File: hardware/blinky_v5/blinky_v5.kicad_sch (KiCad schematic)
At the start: 235 parts, among them J1 RJ45, J10 Conn_01x04, J11 Conn_01x08, J12 Conn_01x06, J2 Conn_01x06_Pin, J3 Conn_01x05_Pin, J5 Conn_01x06_Pin, J6 Conn_01x04_Pin, J7 Conn_01x04_Pin, J8 Conn_01x02, J9 Conn_02x10_Odd_Even, Q1 2N7002, Q2 2N7002, Q3 2N7002, Q4 2N7002, Q5 2N7002, Q6 2N7002, Q7 2N7002, Q8 2N7002, U1 ADA4807-1, U10 STM32F405RGTx, U11 AMS1117-3.3, U12 BA50DD0WHFP-TR, U13 M24C02-RMN, U2 SN74LVC1G14DBV, U3 SN74LVC1G14DBV, U4 ADA4807-1, U5 ADA4807-1, U6 TLV3603DCKR, U7 SN74LVC1G14DBV, U8 TLV3603DCKR, U9 L78L05_SOT89, X1 GTXO-14V (2.048MHz), X2 GTXO-14V (2.048MHz), Y1 AOCJY4A-10.000MHZ-SW, Y2 16MHz

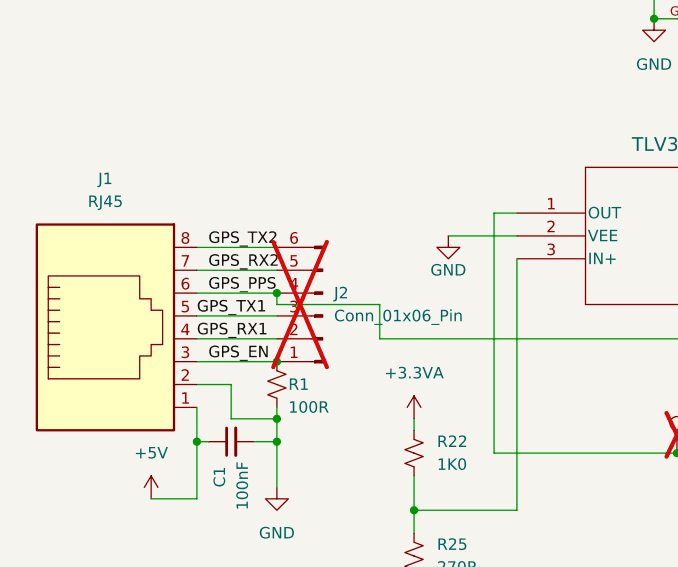
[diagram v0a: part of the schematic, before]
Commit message: fix GPS PPS routing bug
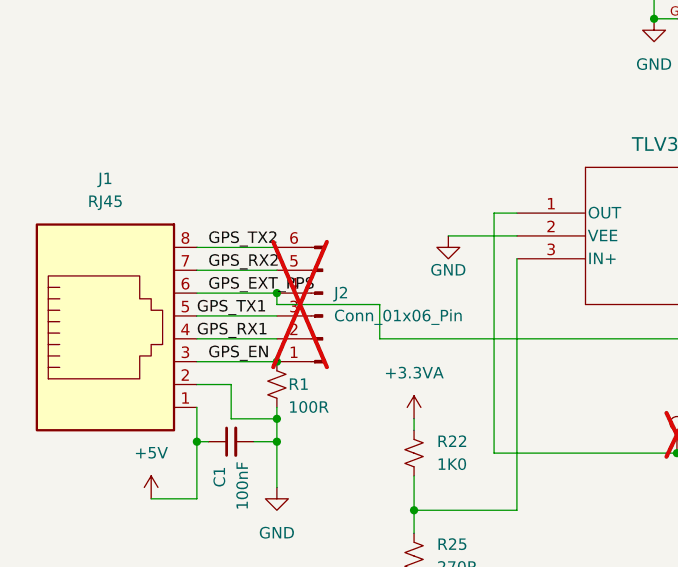
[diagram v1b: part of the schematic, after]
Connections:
- net GPS_PPS: no longer J1.6, J2.4 (Pin_4), U8.4 (IN-)
- new net GPS_EXT_PPS: J1.6, J2.4 (Pin_4), U8.4 (IN-)

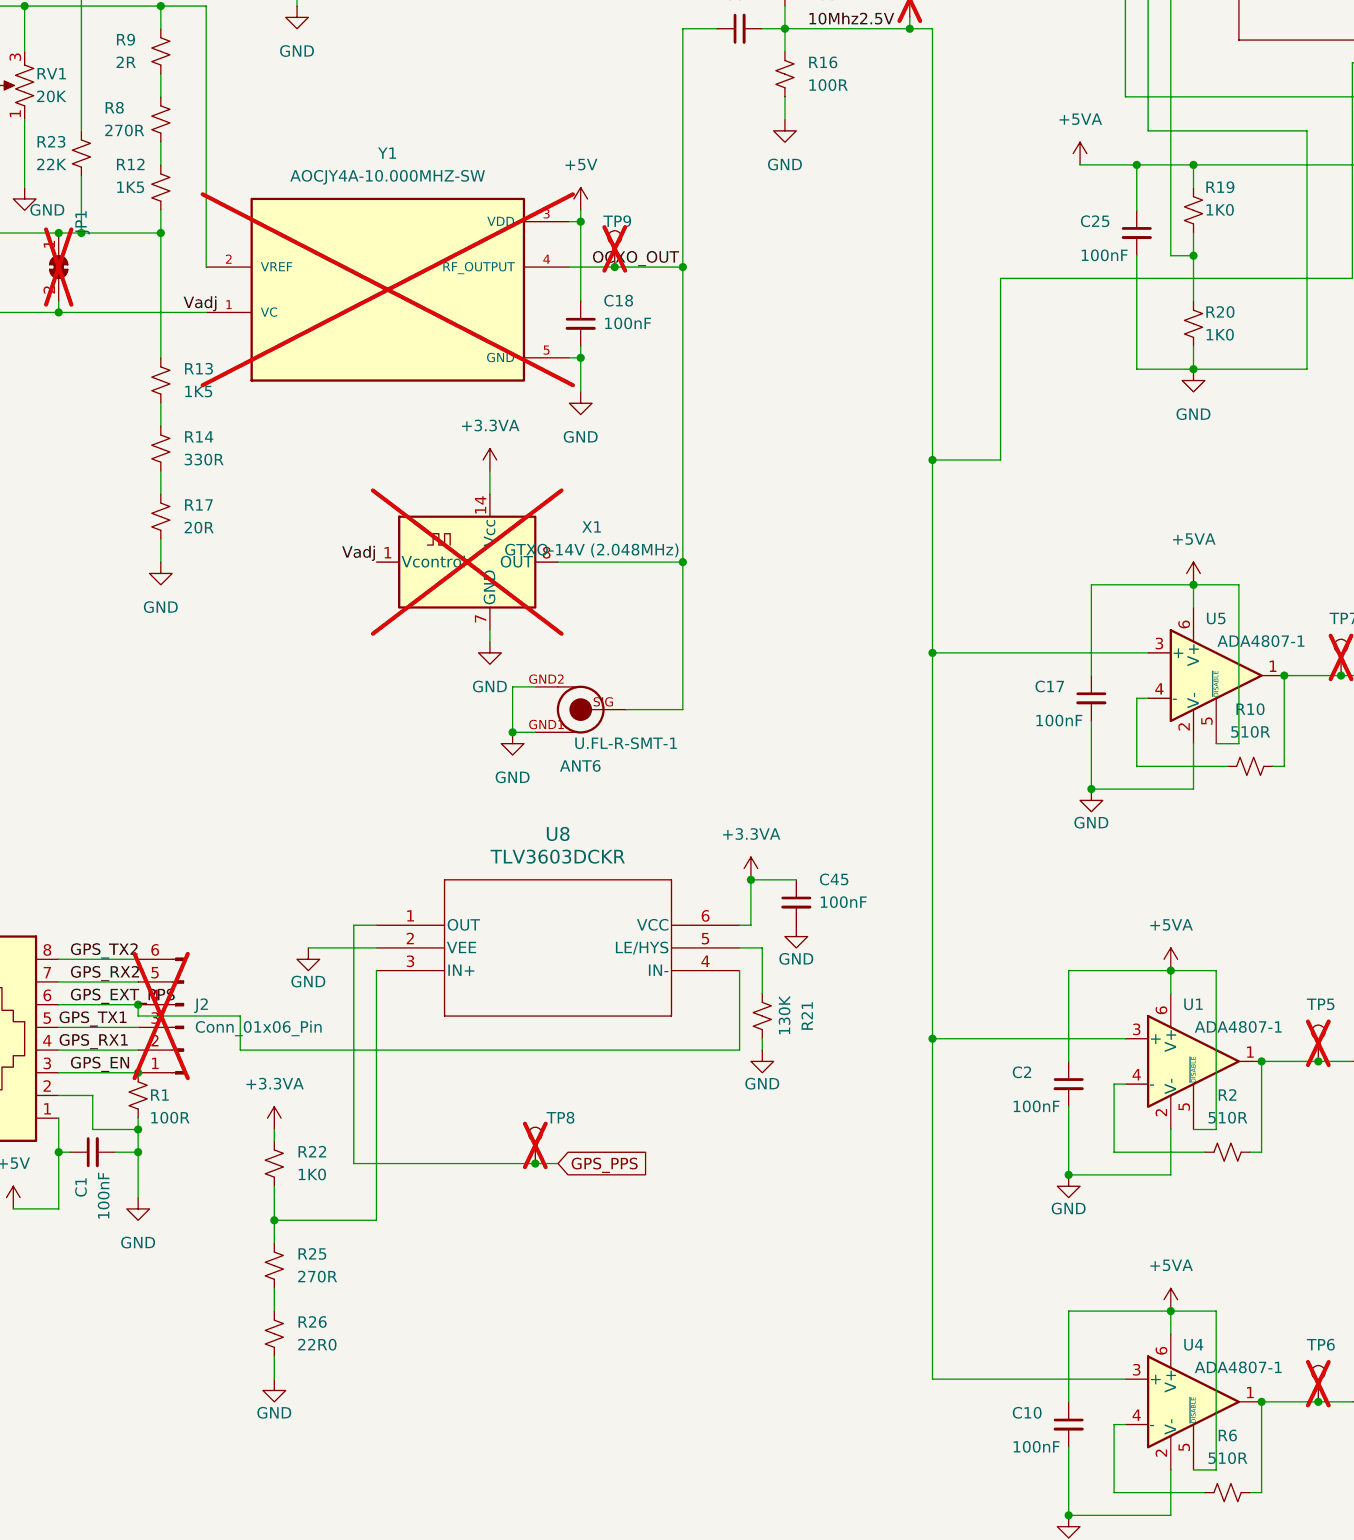
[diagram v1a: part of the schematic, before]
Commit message: filter power splits
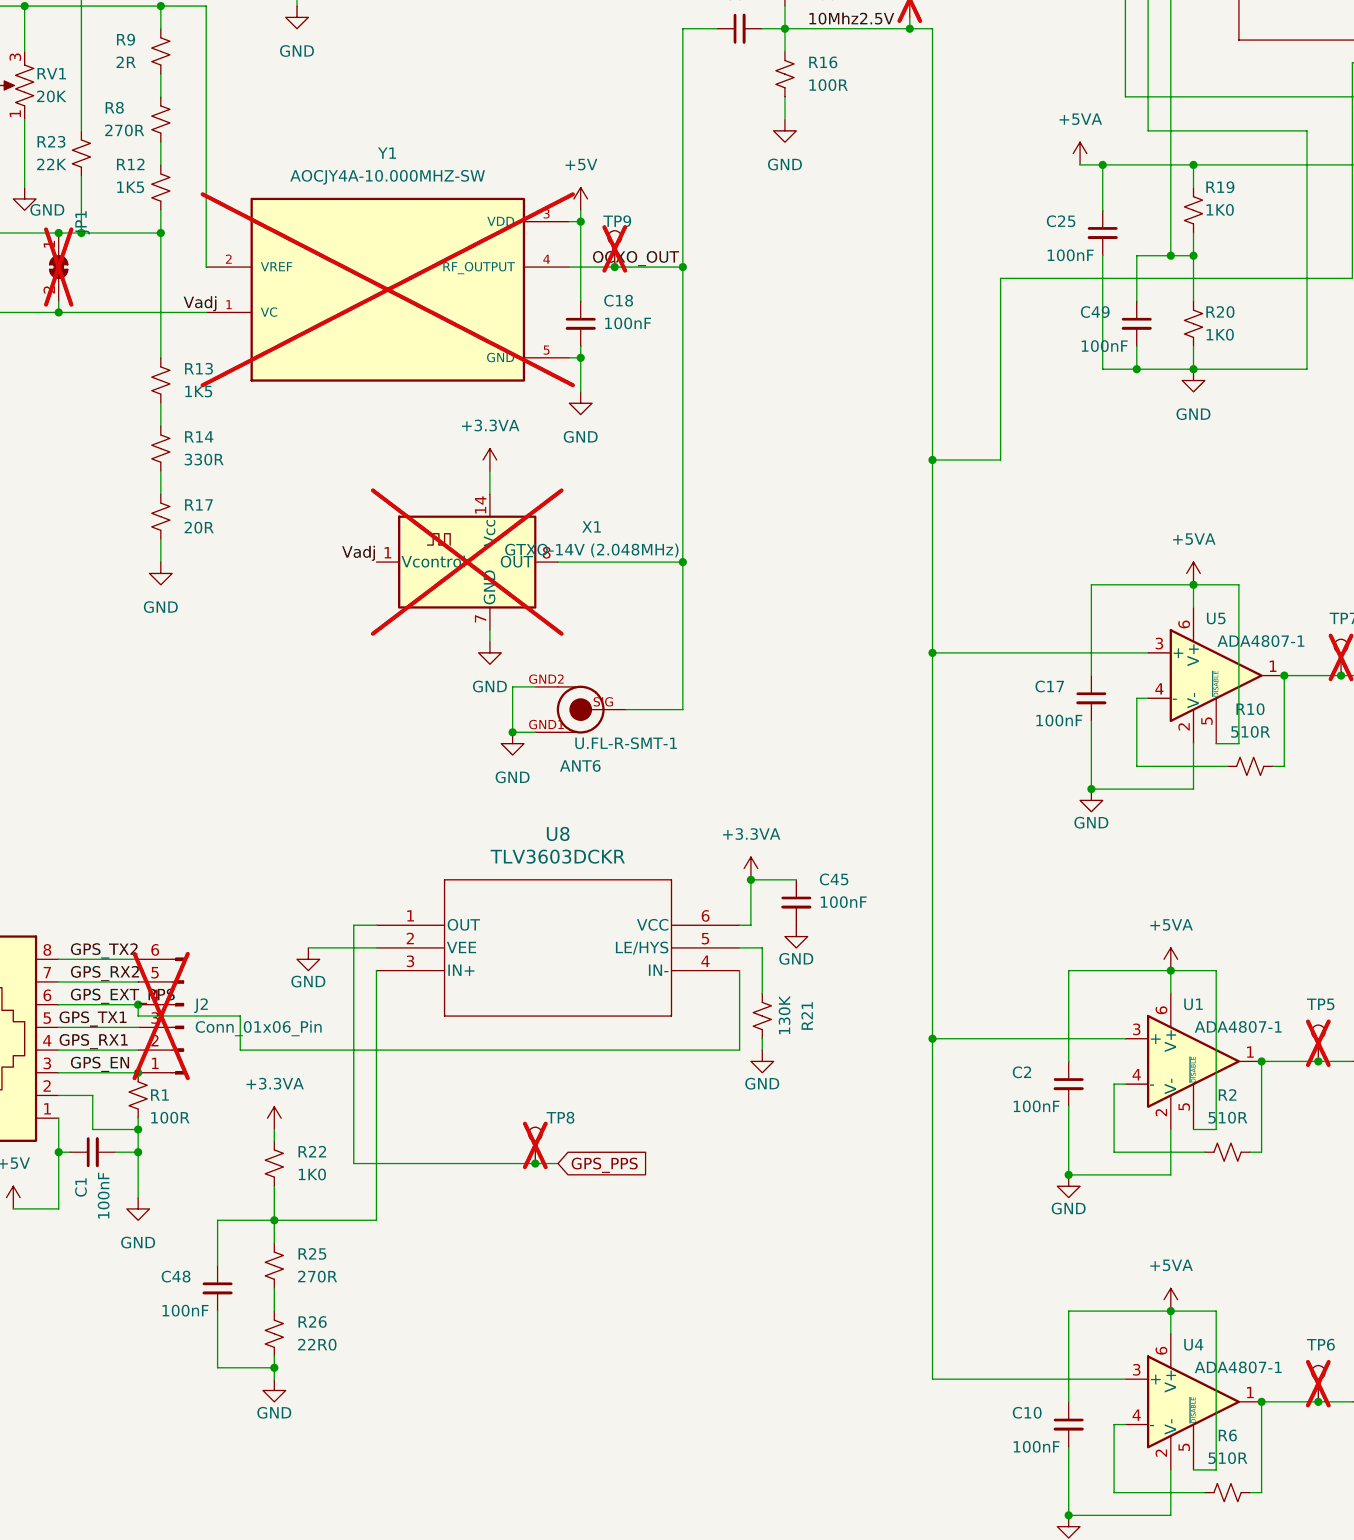
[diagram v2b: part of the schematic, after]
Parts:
- added C48, C49: 100nF, Capacitor_SMD:C_0402_1005Metric, symbol Device:C_Small
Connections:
- net GND: now also C48.2, C49.2
- net at R22.2, R25.1, U8.3 (IN+): now also C48.1
- net at R19.2, R20.1, U6.3 (IN+): now also C49.1
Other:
- moved on the sheet: C25
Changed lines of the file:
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@@
   (junction (at 393.7 132.08) (diameter 0) (color 0 0 0 0)
   )
+  (junction (at 151.13 247.65) (diameter 0) (color 0 0 0 0)
+  )
   (junction (at 359.41 201.93) (diameter 0) (color 0 0 0 0)
   )
@@
   (junction (at 36.83 220.98) (diameter 0) (color 0 0 0 0)
   )
-  (junction (at 154.94 247.65) (diameter 0) (color 0 0 0 0)
-  )
   (junction (at 373.38 132.08) (diameter 0) (color 0 0 0 0)
   )
@@
   (junction (at 308.61 388.62) (diameter 0) (color 0 0 0 0)
   )
+  (junction (at 154.94 270.51) (diameter 0) (color 0 0 0 0)
+  )
   (junction (at 161.29 257.81) (diameter 0) (color 0 0 0 0)
   )
@@
   (junction (at 383.54 132.08) (diameter 0) (color 0 0 0 0)
   )
+  (junction (at 58.42 382.27) (diameter 0) (color 0 0 0 0)
+  )
   (junction (at 288.29 80.01) (diameter 0) (color 0 0 0 0)
   )
   (junction (at 359.41 170.18) (diameter 0) (color 0 0 0 0)
   )
+  (junction (at 158.75 257.81) (diameter 0) (color 0 0 0 0)
+  )
   (junction (at 359.41 215.9) (diameter 0) (color 0 0 0 0)
   )
@@
     (stroke (width 0) (type default))
   )
-  (wire (pts (xy 154.94 247.65) (xy 148.59 247.65))
-    (stroke (width 0) (type default))
-  )
-  (wire (pts (xy 154.94 257.81) (xy 154.94 270.51))
+  (wire (pts (xy 151.13 257.81) (xy 151.13 270.51))
     (stroke (width 0) (type default))
   )
@@
     (stroke (width 0) (type default))
   )
+  (wire (pts (xy 154.94 270.51) (xy 161.29 270.51))
+    (stroke (width 0) (type default))
+  )
   (wire (pts (xy 302.26 295.91) (xy 302.26 298.45))
     (stroke (width 0) (type default))
@@
     (stroke (width 0) (type default))
   )
+  (wire (pts (xy 151.13 247.65) (xy 161.29 247.65))
+    (stroke (width 0) (type default))
+  )
   (wire (pts (xy 332.74 275.59) (xy 334.01 275.59))
     (stroke (width 0) (type default))
@@
     (stroke (width 0) (type default))
   )
+  (wire (pts (xy 154.94 267.97) (xy 154.94 270.51))
+    (stroke (width 0) (type default))
+  )
   (wire (pts (xy 39.37 139.7) (xy 40.64 139.7))
     (stroke (width 0) (type default))
@@
     (stroke (width 0) (type default))
   )
+  (wire (pts (xy 58.42 382.27) (xy 58.42 383.54))
+    (stroke (width 0) (type default))
+  )
   (wire (pts (xy 66.04 86.36) (xy 66.04 87.63))
     (stroke (width 0) (type default))
@@
     (stroke (width 0) (type default))
   )
-  (wire (pts (xy 154.94 270.51) (xy 161.29 270.51))
+  (wire (pts (xy 151.13 270.51) (xy 154.94 270.51))
     (stroke (width 0) (type default))
   )
@@
     (stroke (width 0) (type default))
   )
+  (wire (pts (xy 154.94 257.81) (xy 158.75 257.81))
+    (stroke (width 0) (type default))
+  )
   (wire (pts (xy 363.22 233.68) (xy 355.6 233.68))
     (stroke (width 0) (type default))
@@
     (stroke (width 0) (type default))
   )
+  (wire (pts (xy 52.07 370.84) (xy 52.07 365.76))
+    (stroke (width 0) (type default))
+  )
   (wire (pts (xy 147.32 353.06) (xy 147.32 360.68))
     (stroke (width 0) (type default))
@@
     (stroke (width 0) (type default))
   )
+  (wire (pts (xy 52.07 375.92) (xy 52.07 382.27))
+    (stroke (width 0) (type default))
+  )
   (wire (pts (xy 92.71 254) (xy 92.71 262.89))
     (stroke (width 0) (type default))
@@
     (stroke (width 0) (type default))
   )
+  (wire (pts (xy 52.07 382.27) (xy 58.42 382.27))
+    (stroke (width 0) (type default))
+  )
   (wire (pts (xy 163.83 393.7) (xy 163.83 375.92))
     (stroke (width 0) (type default))
@@
     (stroke (width 0) (type default))
   )
-  (wire (pts (xy 58.42 381) (xy 58.42 383.54))
+  (wire (pts (xy 58.42 381) (xy 58.42 382.27))
     (stroke (width 0) (type default))
   )
@@
     (stroke (width 0) (type default))
   )
+  (wire (pts (xy 154.94 262.89) (xy 154.94 257.81))
+    (stroke (width 0) (type default))
+  )
   (wire (pts (xy 383.54 168.91) (xy 378.46 168.91))
     (stroke (width 0) (type default))
@@
     (stroke (width 0) (type default))
   )
-  (wire (pts (xy 154.94 247.65) (xy 161.29 247.65))
-    (stroke (width 0) (type default))
-  )
   (wire (pts (xy 166.37 294.64) (xy 161.29 294.64))
     (stroke (width 0) (type default))
@@
     (stroke (width 0) (type default))
   )
+  (wire (pts (xy 151.13 247.65) (xy 148.59 247.65))
+    (stroke (width 0) (type default))
+  )
   (wire (pts (xy 320.04 27.94) (xy 320.04 30.48))
     (stroke (width 0) (type default))
@@
     (stroke (width 0) (type default))
   )
+  (wire (pts (xy 52.07 365.76) (xy 58.42 365.76))
+    (stroke (width 0) (type default))
+  )
   (wire (pts (xy 45.72 245.11) (xy 45.72 247.65))
     (stroke (width 0) (type default))
@@
     (stroke (width 0) (type default))
   )
-  (wire (pts (xy 154.94 252.73) (xy 154.94 247.65))
+  (wire (pts (xy 151.13 252.73) (xy 151.13 247.65))
     (stroke (width 0) (type default))
   )
@@
     )
   )
+  (symbol (lib_id "Device:C_Small") (at 52.07 373.38 0) (unit 1)
+    (in_bom yes) (on_board yes) (dnp no)
+    (property "Reference" "C48" (at 45.72 372.11 0)
+      (effects (font (size 1.27 1.27)) (justify left))
+    )
+    (property "Value" "100nF" (at 45.72 375.92 0)
+      (effects (font (size 1.27 1.27)) (justify left))
+    )
+    (property "Footprint" "Capacitor_SMD:C_0402_1005Metric" (at 52.07 373.38 0)
+      (effects (font (size 1.27 1.27)) hide)
+    )
+    (property "Datasheet" "https://www.mouser.ca/datasheet/2/447/UPY_GPHC_X7R_6_3V_to_250V_23-3084653.pdf" (at 52.07 373.38 0)
+      (effects (font (size 1.27 1.27)) hide)
+    )
+    (property "LCSC" "C307331" (at 52.07 373.38 0)
+      (effects (font (size 1.27 1.27)) hide)
+    )
+    (pin "1")
+    (pin "2")
+    (instances
+      (project "blinky_v5"
+        (path "/bd4d3b9a-07c1-4a53-9c94-2893f3e869d4"
+          (reference "C48") (unit 1)
+        )
+      )
+    )
+  )
   (symbol (lib_id "Device:LED") (at 289.56 35.56 90) (unit 1)
     (in_bom yes) (on_board yes) (dnp no) (fields_autoplaced)
@@
     )
   )
-  (symbol (lib_id "Device:C_Small") (at 154.94 255.27 0) (unit 1)
+  (symbol (lib_id "Device:C_Small") (at 151.13 255.27 0) (unit 1)
     (in_bom yes) (on_board yes) (dnp no)
-    (property "Reference" "C25" (at 148.59 254 0)
+    (property "Reference" "C25" (at 144.78 254 0)
       (effects (font (size 1.27 1.27)) (justify left))
     )
-    (property "Value" "100nF" (at 148.59 257.81 0)
+    (property "Value" "100nF" (at 144.78 257.81 0)
       (effects (font (size 1.27 1.27)) (justify left))
     )
-    (property "Footprint" "Capacitor_SMD:C_0402_1005Metric" (at 154.94 255.27 0)
+    (property "Footprint" "Capacitor_SMD:C_0402_1005Metric" (at 151.13 255.27 0)
       (effects (font (size 1.27 1.27)) hide)
     )
-    (property "Datasheet" "https://www.mouser.ca/datasheet/2/447/UPY_GPHC_X7R_6_3V_to_250V_23-3084653.pdf" (at 154.94 255.27 0)
+    (property "Datasheet" "https://www.mouser.ca/datasheet/2/447/UPY_GPHC_X7R_6_3V_to_250V_23-3084653.pdf" (at 151.13 255.27 0)
       (effects (font (size 1.27 1.27)) hide)
     )
-    (property "LCSC" "C307331" (at 154.94 255.27 0)
+    (property "LCSC" "C307331" (at 151.13 255.27 0)
       (effects (font (size 1.27 1.27)) hide)
     )
@@
         )
       )
+    )
+  )
+  (symbol (lib_id "Device:C_Small") (at 154.94 265.43 0) (unit 1)
+    (in_bom yes) (on_board yes) (dnp no)
+    (property "Reference" "C49" (at 148.59 264.16 0)
+      (effects (font (size 1.27 1.27)) (justify left))
+    )
+    (property "Value" "100nF" (at 148.59 267.97 0)
+      (effects (font (size 1.27 1.27)) (justify left))
+    )
+    (property "Footprint" "Capacitor_SMD:C_0402_1005Metric" (at 154.94 265.43 0)
+      (effects (font (size 1.27 1.27)) hide)
+    )
+    (property "Datasheet" "https://www.mouser.ca/datasheet/2/447/UPY_GPHC_X7R_6_3V_to_250V_23-3084653.pdf" (at 154.94 265.43 0)
+      (effects (font (size 1.27 1.27)) hide)
+    )
+    (property "LCSC" "C307331" (at 154.94 265.43 0)
+      (effects (font (size 1.27 1.27)) hide)
+    )
+    (pin "1")
+    (pin "2")
+    (instances
+      (project "blinky_v5"
+        (path "/bd4d3b9a-07c1-4a53-9c94-2893f3e869d4"
+          (reference "C49") (unit 1)
+        )
+      )

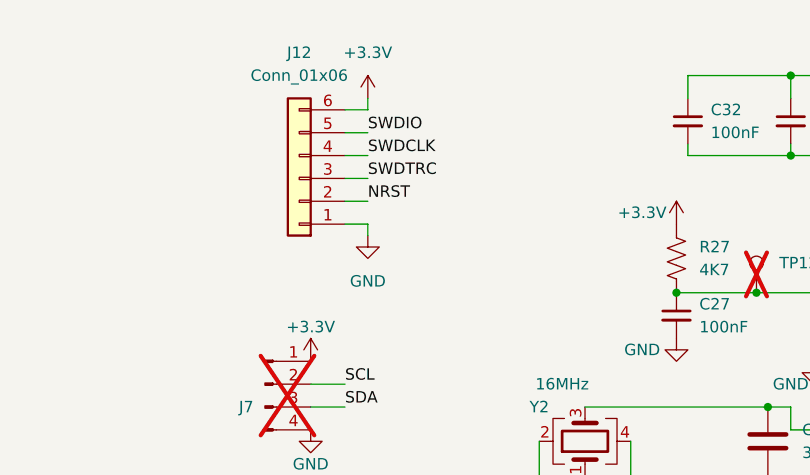
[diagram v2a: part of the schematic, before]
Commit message: put the serial ouput on connector
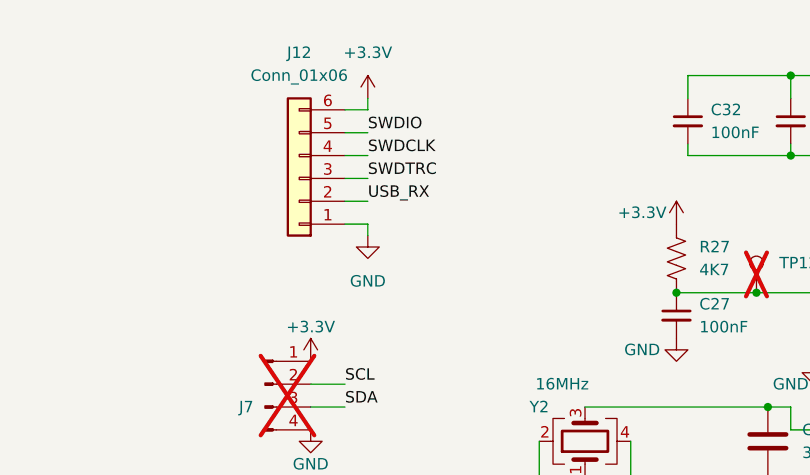
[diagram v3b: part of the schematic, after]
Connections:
- net NRST: no longer J12.2 (Pin_2)
- net USB_RX: now also J12.2 (Pin_2)
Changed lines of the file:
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@@
     (effects (font (size 1.27 1.27)) (justify left bottom))
   )
-  (label "NRST" (at 124.46 43.18 0) (fields_autoplaced)
+  (label "USB_RX" (at 124.46 43.18 0) (fields_autoplaced)
     (effects (font (size 1.27 1.27)) (justify left bottom))
   )
